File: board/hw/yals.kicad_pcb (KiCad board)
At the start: 2 copper layers, 102.9 x 16.5 mm, 42 parts, among them J1 SWD, J2 UART, J3 eng, J4 power, U1 RP2040, U2 M24C02-FMN, U3 MCP1703Ax-330xxTT, U4 W25Q32JVSS, U5 DRV8220, U6 LM321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

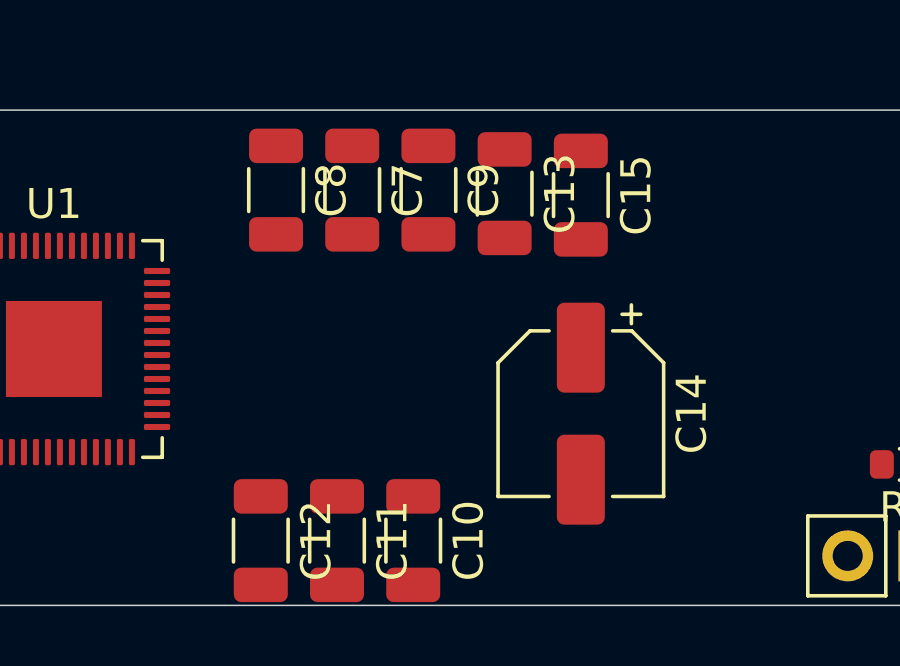
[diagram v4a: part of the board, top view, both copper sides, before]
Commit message: monior repositioning to avoid PCB edges and better alignment of parallel elements
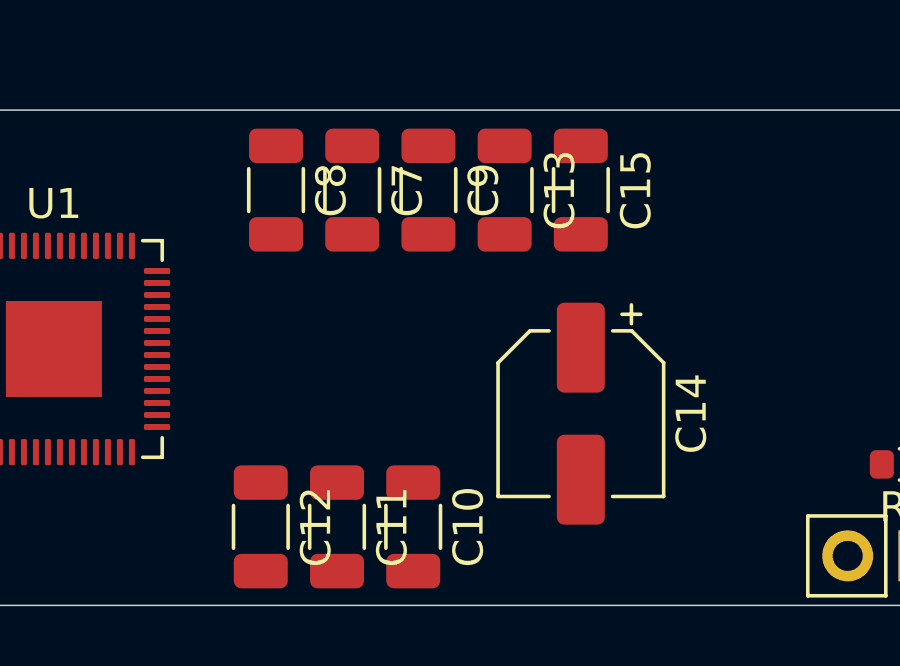
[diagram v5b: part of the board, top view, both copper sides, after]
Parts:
- moved C10 0.46 mm to (141.2, 92.0)
- moved C11 0.46 mm to (138.7, 92.0)
- moved C12 0.46 mm to (136.1, 92.0)
- moved C15 0.17 mm to (146.8, 80.8)
- moved C13 0.12 mm to (144.3, 80.8)
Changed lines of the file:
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@@
   )
   (footprint "Capacitor_SMD:C_1206_3216Metric" (layer "F.Cu")
-    (at 136.144 92.456 -90)
+    (at 136.144 91.997 -90)
     (descr "Capacitor SMD 1206 (3216 Metric), square (rectangular) end terminal, IPC_7351 nominal, (Body size source: IPC-SM-782 page 76, https://www.pcb-3d.com/wordpress/wp-content/uploads/ipc-sm-782a_amendment_1_and_2.pdf), generated with kicad-footprint-generator")
     (tags "capacitor")
@@
   )
   (footprint "Capacitor_SMD:C_1206_3216Metric" (layer "F.Cu")
-    (at 144.272 80.891 -90)
+    (at 144.272 80.772 -90)
     (descr "Capacitor SMD 1206 (3216 Metric), square (rectangular) end terminal, IPC_7351 nominal, (Body size source: IPC-SM-782 page 76, https://www.pcb-3d.com/wordpress/wp-content/uploads/ipc-sm-782a_amendment_1_and_2.pdf), generated with kicad-footprint-generator")
     (tags "capacitor")
@@
   )
   (footprint "Capacitor_SMD:C_1206_3216Metric" (layer "F.Cu")
-    (at 146.812 80.94 -90)
+    (at 146.812 80.772 -90)
     (descr "Capacitor SMD 1206 (3216 Metric), square (rectangular) end terminal, IPC_7351 nominal, (Body size source: IPC-SM-782 page 76, https://www.pcb-3d.com/wordpress/wp-content/uploads/ipc-sm-782a_amendment_1_and_2.pdf), generated with kicad-footprint-generator")
     (tags "capacitor")
@@
   )
   (footprint "Capacitor_SMD:C_1206_3216Metric" (layer "F.Cu")
-    (at 141.224 92.456 -90)
+    (at 141.224 91.997 -90)
     (descr "Capacitor SMD 1206 (3216 Metric), square (rectangular) end terminal, IPC_7351 nominal, (Body size source: IPC-SM-782 page 76, https://www.pcb-3d.com/wordpress/wp-content/uploads/ipc-sm-782a_amendment_1_and_2.pdf), generated with kicad-footprint-generator")
     (tags "capacitor")
@@
   )
   (footprint "Capacitor_SMD:C_1206_3216Metric" (layer "F.Cu")
-    (at 138.684 92.456 -90)
+    (at 138.684 91.997 -90)
     (descr "Capacitor SMD 1206 (3216 Metric), square (rectangular) end terminal, IPC_7351 nominal, (Body size source: IPC-SM-782 page 76, https://www.pcb-3d.com/wordpress/wp-content/uploads/ipc-sm-782a_amendment_1_and_2.pdf), generated with kicad-footprint-generator")
     (tags "capacitor")

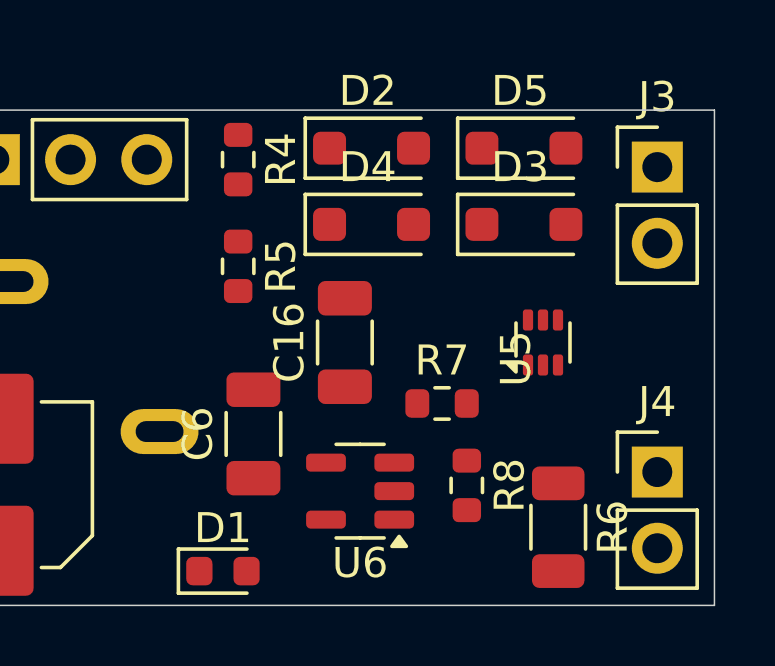
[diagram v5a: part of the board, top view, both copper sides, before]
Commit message: main power line and engine power routed
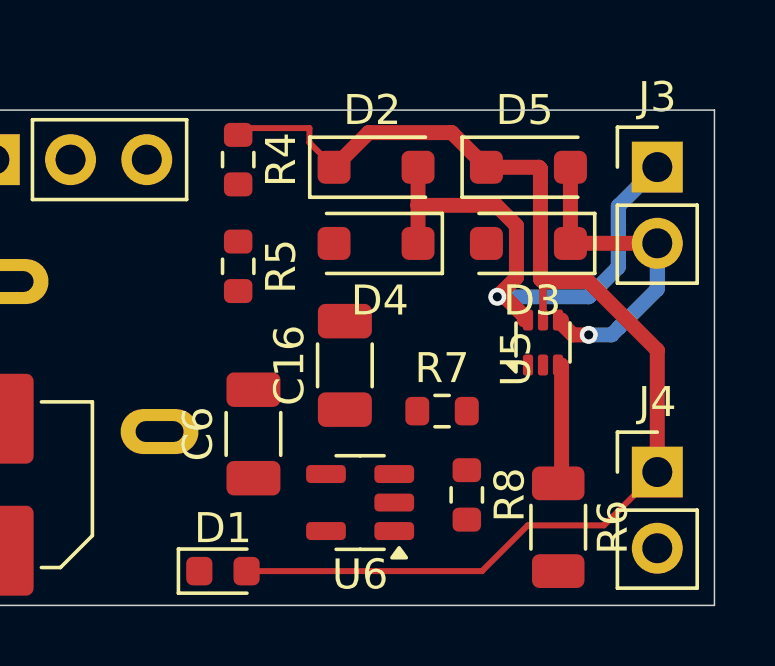
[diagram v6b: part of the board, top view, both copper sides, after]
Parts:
- moved C16 0.76 mm to (181.4, 86.6)
- moved D5 0.65 mm to (187.5, 80.0)
- moved D2 0.65 mm to (182.4, 80.0)
- moved D3 0.65 mm to (187.5, 82.5), turned to 180 degrees
- moved D4 0.65 mm to (182.4, 82.5), turned to 180 degrees
- moved U6 0.38 mm to (181.9, 91.2)
- moved R8 0.32 mm to (185.4, 90.9)
- moved R7 0.25 mm to (184.6, 88.1)
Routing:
- net +12V: track 0.00 -> 40.9 mm
- net Net-(D2-A): track 0.00 -> 18.4 mm, vias 0 -> 1
- net Net-(D3-K): track 0.00 -> 11.1 mm, vias 0 -> 1
- net Net-(U5-GND): track 0.00 -> 3.99 mm
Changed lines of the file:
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@@
   )
   (footprint "Diode_SMD:D_SOD-123F" (layer "F.Cu")
-    (at 187.325 81.915)
+    (at 187.4744 82.55 180)
     (descr "D_SOD-123F")
     (tags "D_SOD-123F")
@@
     (fp_line (start 1.4 0.9) (end -1.4 0.9)
       (stroke (width 0.1) (type solid)) (layer "F.Fab"))
-    (pad "1" smd roundrect (at -1.4 0) (size 1.1 1.1) (layers "F.Cu" "F.Paste" "F.Mask") (roundrect_rratio 0.2272727273)
+    (pad "1" smd roundrect (at -1.4 0 180) (size 1.1 1.1) (layers "F.Cu" "F.Paste" "F.Mask") (roundrect_rratio 0.2272727273)
       (net 53 "Net-(D3-K)") (pinfunction "K") (pintype "passive"))
-    (pad "2" smd roundrect (at 1.4 0) (size 1.1 1.1) (layers "F.Cu" "F.Paste" "F.Mask") (roundrect_rratio 0.2272727273)
+    (pad "2" smd roundrect (at 1.4 0 180) (size 1.1 1.1) (layers "F.Cu" "F.Paste" "F.Mask") (roundrect_rratio 0.2272727273)
       (net 35 "GND") (pinfunction "A") (pintype "passive"))
     (model "${KICAD6_3DMODEL_DIR}/Diode_SMD.3dshapes/D_SOD-123F.wrl"
@@
   )
   (footprint "Package_TO_SOT_SMD:SOT-23-5" (layer "F.Cu")
-    (at 181.864 90.806 180)
+    (at 181.864 91.186 180)
     (descr "SOT, 5 Pin (https://www.jedec.org/sites/default/files/docs/Mo-178c.PDF variant AA), generated with kicad-footprint-generator ipc_gullwing_generator.py")
     (tags "SOT TO_SOT_SMD")
@@
   )
   (footprint "Diode_SMD:D_SOD-123F" (layer "F.Cu")
-    (at 182.245 81.915)
+    (at 182.3944 82.55 180)
     (descr "D_SOD-123F")
     (tags "D_SOD-123F")
@@
     (fp_line (start 1.4 0.9) (end -1.4 0.9)
       (stroke (width 0.1) (type solid)) (layer "F.Fab"))
-    (pad "1" smd roundrect (at -1.4 0) (size 1.1 1.1) (layers "F.Cu" "F.Paste" "F.Mask") (roundrect_rratio 0.2272727273)
+    (pad "1" smd roundrect (at -1.4 0 180) (size 1.1 1.1) (layers "F.Cu" "F.Paste" "F.Mask") (roundrect_rratio 0.2272727273)
       (net 52 "Net-(D2-A)") (pinfunction "K") (pintype "passive"))
-    (pad "2" smd roundrect (at 1.4 0) (size 1.1 1.1) (layers "F.Cu" "F.Paste" "F.Mask") (roundrect_rratio 0.2272727273)
+    (pad "2" smd roundrect (at 1.4 0 180) (size 1.1 1.1) (layers "F.Cu" "F.Paste" "F.Mask") (roundrect_rratio 0.2272727273)
       (net 35 "GND") (pinfunction "A") (pintype "passive"))
     (model "${KICAD6_3DMODEL_DIR}/Diode_SMD.3dshapes/D_SOD-123F.wrl"
@@
   )
   (footprint "Resistor_SMD:R_0603_1608Metric" (layer "F.Cu")
-    (at 185.42 90.615 -90)
+    (at 185.42 90.932 -90)
     (descr "Resistor SMD 0603 (1608 Metric), square (rectangular) end terminal, IPC_7351 nominal, (Body size source: IPC-SM-782 page 72, https://www.pcb-3d.com/wordpress/wp-content/uploads/ipc-sm-782a_amendment_1_and_2.pdf), generated with kicad-footprint-generator")
     (tags "resistor")
@@
   )
   (footprint "Diode_SMD:D_SOD-123F" (layer "F.Cu")
-    (at 182.245 79.375)
+    (at 182.3944 80.01)
     (descr "D_SOD-123F")
     (tags "D_SOD-123F")
@@
   )
   (footprint "Diode_SMD:D_SOD-123F" (layer "F.Cu")
-    (at 187.325 79.375)
+    (at 187.4744 80.01)
     (descr "D_SOD-123F")
     (tags "D_SOD-123F")
@@
   )
   (footprint "Resistor_SMD:R_0603_1608Metric" (layer "F.Cu")
-    (at 184.595 87.884)
+    (at 184.595 88.138)
     (descr "Resistor SMD 0603 (1608 Metric), square (rectangular) end terminal, IPC_7351 nominal, (Body size source: IPC-SM-782 page 72, https://www.pcb-3d.com/wordpress/wp-content/uploads/ipc-sm-782a_amendment_1_and_2.pdf), generated with kicad-footprint-generator")
     (tags "resistor")
@@
   )
   (footprint "Capacitor_SMD:C_1206_3216Metric" (layer "F.Cu")
-    (at 181.356 85.852 90)
+    (at 181.356 86.614 90)
     (descr "Capacitor SMD 1206 (3216 Metric), square (rectangular) end terminal, IPC_7351 nominal, (Body size source: IPC-SM-782 page 76, https://www.pcb-3d.com/wordpress/wp-content/uploads/ipc-sm-782a_amendment_1_and_2.pdf), generated with kicad-footprint-generator")
     (tags "capacitor")
@@
   (gr_line (start 90.805 94.615) (end 193.675 94.615)
     (stroke (width 0.05) (type default)) (layer "Edge.Cuts"))
+  (segment (start 189.992 91.948) (end 191.77 90.17) (width 0.2) (layer "F.Cu") (net 36))
+  (segment (start 180.175 78.705) (end 180.175 79.1906) (width 0.2) (layer "F.Cu") (net 36))
+  (segment (start 178.0795 93.472) (end 185.928 93.472) (width 0.2) (layer "F.Cu") (net 36))
+  (segment (start 186.0744 80.01) (end 184.9194 78.855) (width 0.5) (layer "F.Cu") (net 36))
+  (segment (start 187.8744 80.0608) (end 187.8744 83.7344) (width 0.5) (layer "F.Cu") (net 36))
+  (segment (start 180.175 79.1906) (end 180.9944 80.01) (width 0.2) (layer "F.Cu") (net 36))
+  (segment (start 187.8236 80.01) (end 187.8744 80.0608) (width 0.5) (layer "F.Cu") (net 36))
+  (segment (start 180.175 78.705) (end 178.026 78.705) (width 0.2) (layer "F.Cu") (net 36))
+  (segment (start 186.0744 80.01) (end 187.8236 80.01) (width 0.5) (layer "F.Cu") (net 36))
+  (segment (start 191.77 90.17) (end 191.77 86.106) (width 0.5) (layer "F.Cu") (net 36))
+  (segment (start 191.77 86.106) (end 189.484 83.82) (width 0.5) (layer "F.Cu") (net 36))
+  (segment (start 184.9194 78.855) (end 182.1494 78.855) (width 0.5) (layer "F.Cu") (net 36))
+  (segment (start 189.484 83.82) (end 187.96 83.82) (width 0.5) (layer "F.Cu") (net 36))
+  (segment (start 182.1494 78.855) (end 180.9944 80.01) (width 0.5) (layer "F.Cu") (net 36))
+  (segment (start 187.96 85.102) (end 187.96 83.82) (width 0.25) (layer "F.Cu") (net 36))
+  (segment (start 185.928 93.472) (end 187.452 91.948) (width 0.2) (layer "F.Cu") (net 36))
+  (segment (start 178.026 78.705) (end 177.8 78.931) (width 0.2) (layer "F.Cu") (net 36))
+  (segment (start 187.8744 83.7344) (end 187.96 83.82) (width 0.5) (layer "F.Cu") (net 36))
+  (segment (start 187.452 91.948) (end 189.992 91.948) (width 0.2) (layer "F.Cu") (net 36))
+  (segment (start 188.58 90.435) (end 188.58 86.602) (width 0.5) (layer "F.Cu") (net 50))
+  (segment (start 188.468 90.547) (end 188.58 90.435) (width 0.5) (layer "F.Cu") (net 50))
+  (segment (start 183.7944 80.01) (end 183.7944 81.28) (width 0.5) (layer "F.Cu") (net 52))
+  (segment (start 187.0744 81.953122) (end 186.401278 81.28) (width 0.5) (layer "F.Cu") (net 52))
+  (segment (start 187.0744 83.6896) (end 187.0744 81.953122) (width 0.5) (layer "F.Cu") (net 52))
+  (segment (start 183.7944 81.28) (end 183.7944 82.55) (width 0.5) (layer "F.Cu") (net 52))
+  (segment (start 186.436 84.328) (end 187.0744 83.6896) (width 0.5) (layer "F.Cu") (net 52))
+  (segment (start 187.34 84.982) (end 187.34 85.102) (width 0.5) (layer "F.Cu") (net 52))
+  (segment (start 186.401278 81.28) (end 183.7944 81.28) (width 0.5) (layer "F.Cu") (net 52))
+  (segment (start 186.436 84.328) (end 186.686 84.328) (width 0.5) (layer "F.Cu") (net 52))
+  (segment (start 186.686 84.328) (end 187.34 84.982) (width 0.5) (layer "F.Cu") (net 52))
+  (via (at 186.436 84.328) (size 0.6) (drill 0.3) (layers "F.Cu" "B.Cu") (net 52))
+  (segment (start 190.47 83.342) (end 189.484 84.328) (width 0.5) (layer "B.Cu") (net 52))
+  (segment (start 191.77 80.005) (end 190.47 81.305) (width 0.5) (layer "B.Cu") (net 52))
+  (segment (start 189.484 84.328) (end 186.436 84.328) (width 0.5) (layer "B.Cu") (net 52))
+  (segment (start 190.47 81.305) (end 190.47 83.342) (width 0.5) (layer "B.Cu") (net 52))
+  (segment (start 188.8744 80.01) (end 188.8744 82.55) (width 0.5) (layer "F.Cu") (net 53))
+  (segment (start 188.8794 82.545) (end 188.8744 82.55) (width 0.5) (layer "F.Cu") (net 53))
+  (segment (start 188.956 85.598) (end 188.58 85.222) (width 0.5) (layer "F.Cu") (net 53))
+  (segment (start 188.58 85.222) (end 188.58 85.102) (width 0.5) (layer "F.Cu") (net 53))
+  (segment (start 189.484 85.598) (end 188.956 85.598) (width 0.5) (layer "F.Cu") (net 53))
+  (segment (start 191.77 82.545) (end 188.8794 82.545) (width 0.5) (layer "F.Cu") (net 53))
+  (via (at 189.484 85.598) (size 0.6) (drill 0.3) (layers "F.Cu" "B.Cu") (net 53))
+  (segment (start 191.77 84.074) (end 190.5 85.344) (width 0.5) (layer "B.Cu") (net 53))
+  (segment (start 191.77 82.545) (end 191.77 84.074) (width 0.5) (layer "B.Cu") (net 53))
+  (segment (start 190.246 85.598) (end 189.484 85.598) (width 0.5) (layer "B.Cu") (net 53))
+  (segment (start 190.5 85.344) (end 190.246 85.598) (width 0.5) (layer "B.Cu") (net 53))
 )

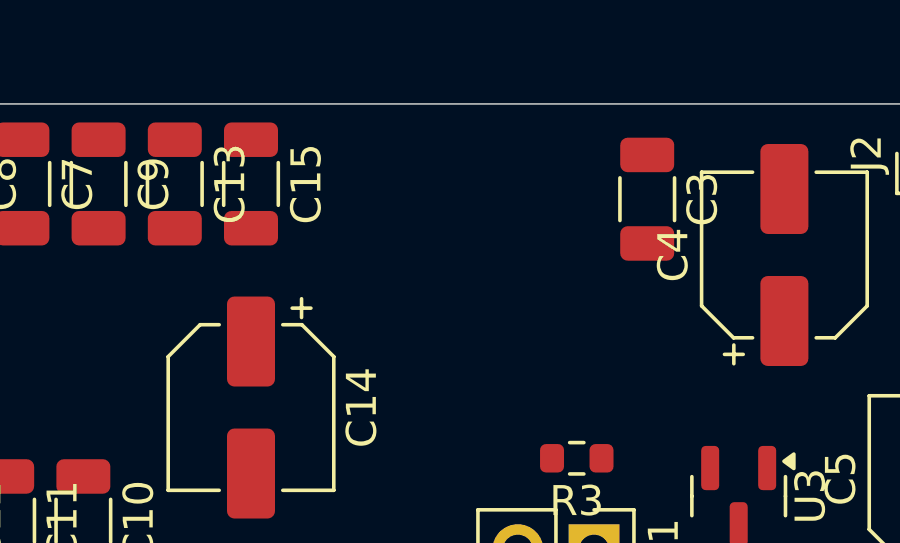
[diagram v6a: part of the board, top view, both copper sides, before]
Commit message: added green LED, controllable from µC
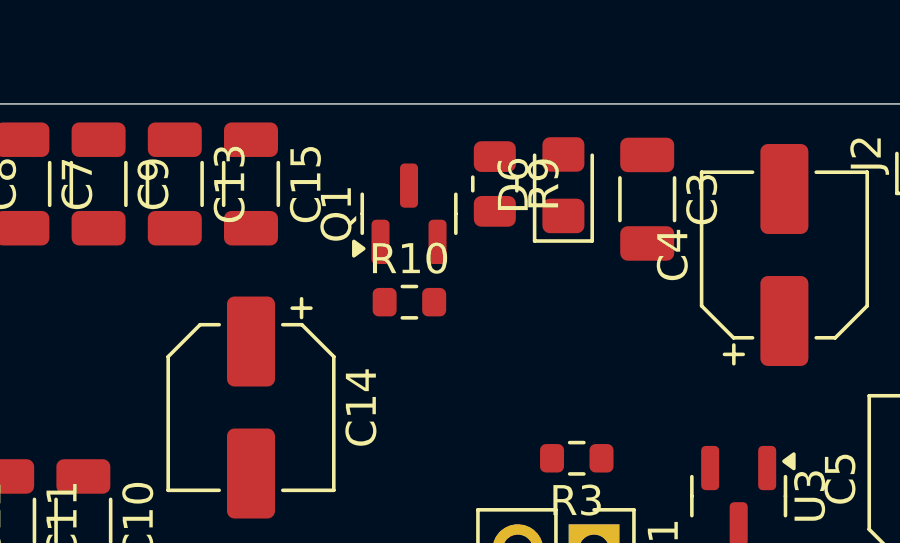
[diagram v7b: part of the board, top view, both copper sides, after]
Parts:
- added D6: LED green, LED_SMD:LED_0805_2012Metric_Pad1.15x1.40mm_HandSolder, F.Cu at (157.2, 80.8)
- added Q1: 2N7002, Package_TO_SOT_SMD:SOT-23, F.Cu at (152.1, 81.8)
- added R10: 100k, Resistor_SMD:R_0603_1608Metric, F.Cu at (152.1, 84.7)
- added R9: 330R, Resistor_SMD:R_0805_2012Metric, F.Cu at (154.9, 80.8)
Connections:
- U1 pad 6: unconnected-(U1-GPIO4-Pad6) -> Net-(Q1-G)

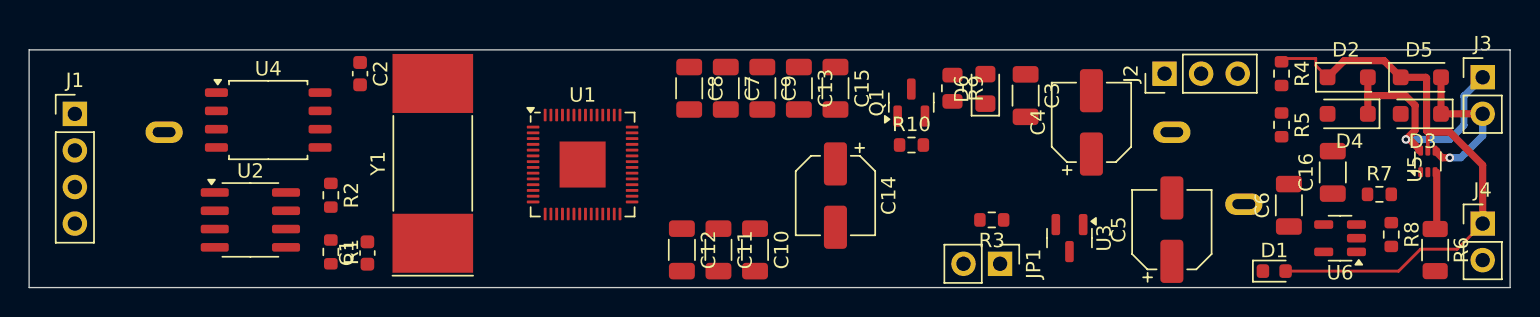
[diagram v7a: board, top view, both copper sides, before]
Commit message: added top+bottom GND plane
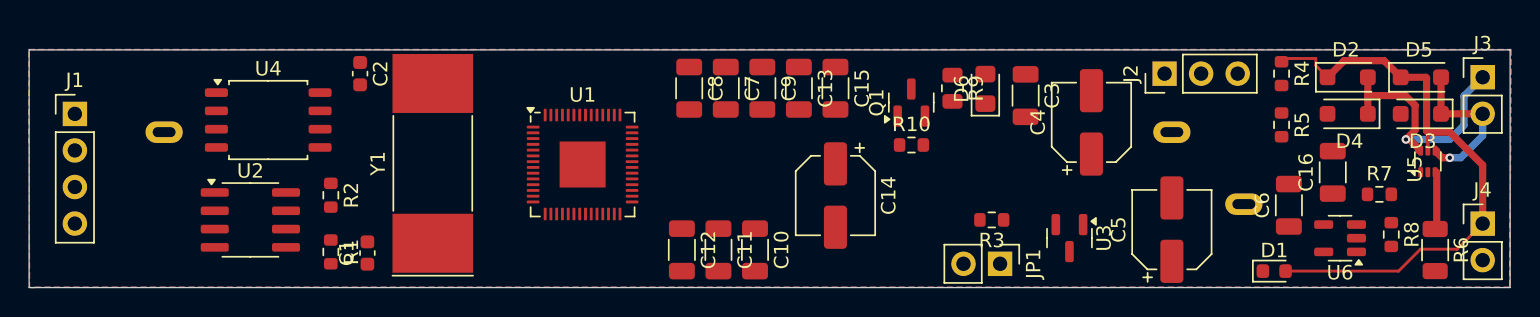
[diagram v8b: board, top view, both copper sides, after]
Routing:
- added copper zone on B.Cu, net GND
- added copper zone on F.Cu, net GND
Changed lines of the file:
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@@
   (segment (start 190.246 85.598) (end 189.484 85.598) (width 0.5) (layer "B.Cu") (net 52))
   (segment (start 190.5 85.344) (end 190.246 85.598) (width 0.5) (layer "B.Cu") (net 52))
+  (zone (net 34) (net_name "GND") (layers "F&B.Cu") (hatch edge 0.5)
+    (connect_pads (clearance 0.5))
+    (min_thickness 0.25) (filled_areas_thickness no)
+    (fill (thermal_gap 0.5) (thermal_bridge_width 0.5))
+    (polygon
+      (pts
+        (xy 90.8304 94.6404)
+        (xy 90.7796 78.0796)
+        (xy 193.7512 78.0796)
+        (xy 193.6496 94.5896)
+        (xy 91.3892 94.5896)
+      )
+    )
+  )
 )
